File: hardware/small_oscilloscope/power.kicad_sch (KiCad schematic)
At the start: 16 parts, among them U10 EA2208T6R, U11 NE555P

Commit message: 250627 circuit
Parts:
- C3: renamed from C7; footprint (none) -> Capacitor_SMD:C_1206_3216Metric_Pad1.33x1.80mm_HandSolder
- C4: renamed from C8; footprint (none) -> Capacitor_SMD:C_0402_1005Metric_Pad0.74x0.62mm_HandSolder
- D1: renamed from D3; footprint Diode_SMD:D_MiniMELF_Handsoldering -> Diode_SMD:D_SOD-123
- D2: footprint Diode_SMD:D_MiniMELF_Handsoldering -> Diode_SMD:D_SOD-123
- D3: renamed from D1; footprint Diode_THT:D_DO-41_SOD81_P10.16mm_Horizontal -> Diode_SMD:D_SOD-123
- R24: footprint (none) -> Resistor_THT:R_Axial_DIN0207_L6.3mm_D2.5mm_P10.16mm_Horizontal
- R25: footprint (none) -> Capacitor_SMD:C_0402_1005Metric_Pad0.74x0.62mm_HandSolder
- renumbered C11 to C5, C10 to C6, C3 to C7, L2 to L1, R21 to R26, R22 to R27, U11 to U9
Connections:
- net +3.3V: no longer L1.1, U10.5 (NC)
- net 5V: now reaches U10.5 (NC)
- net 5V: now also L1.1

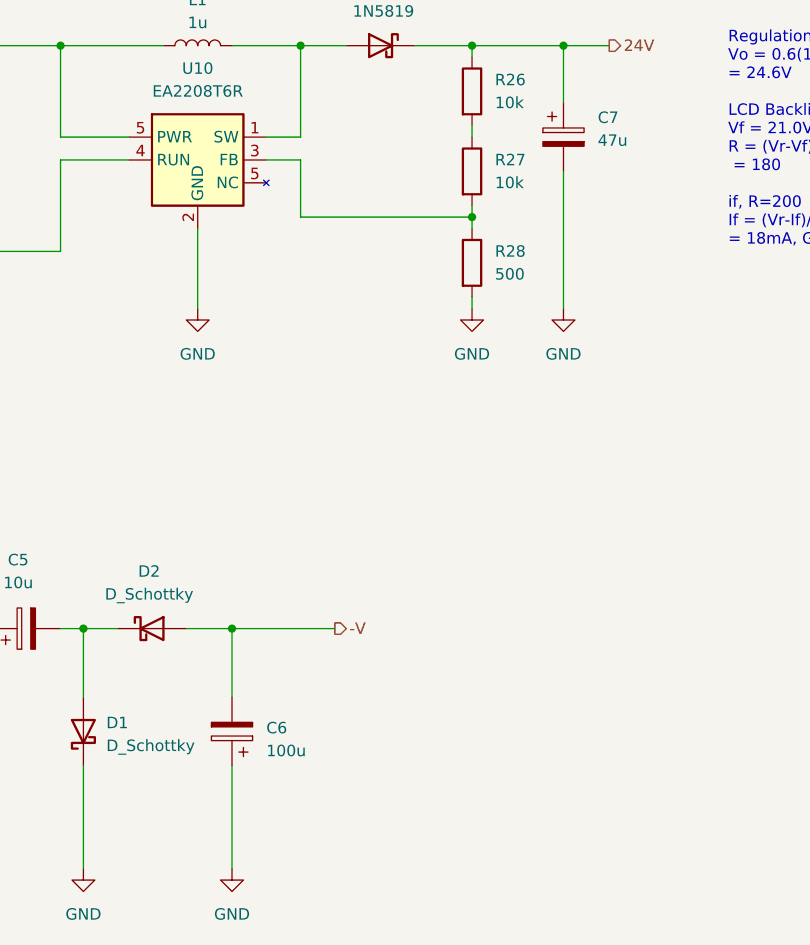
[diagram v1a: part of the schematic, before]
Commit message: feat: 오실로스코프 회로 설계 업데이트
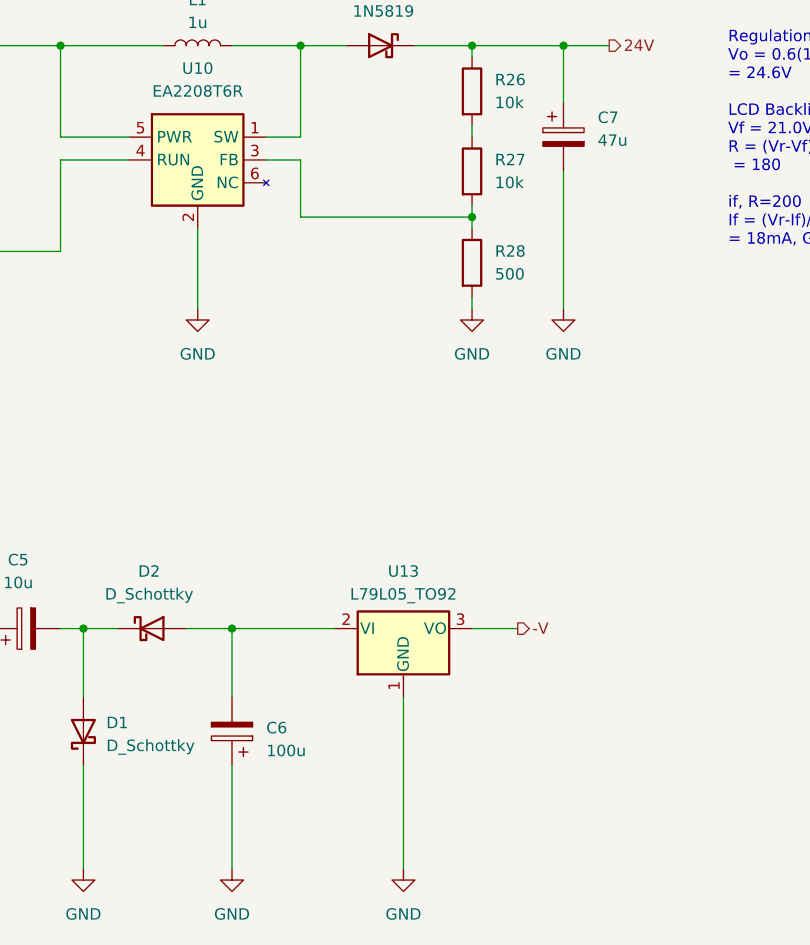
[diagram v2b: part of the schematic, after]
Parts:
- added U13: L79L05_TO92, Package_TO_SOT_THT:TO-92_Inline, symbol Regulator_Linear:L79L05_TO92
- C5: footprint Capacitor_THT:CP_Radial_D5.0mm_P2.00mm -> Capacitor_SMD:CP_Elec_4x5.7
- C6, C7: footprint Capacitor_THT:CP_Radial_D5.0mm_P2.00mm -> Capacitor_SMD:CP_Elec_6.3x5.7
- U9: footprint Package_SO:SOIC-8_3.9x4.9mm_P1.27mm -> Package_DIP:DIP-8_W7.62mm_LongPads
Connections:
- net -V: now also U13.3 (VO); no longer C6.2, D2.2 (A)
- net GND: now also U13.1 (GND)
- new net: C6.2, D2.2 (A), U13.2 (VI)
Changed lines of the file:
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@@
+	(wire
+		(pts
+			(xy 143.51 140.97) (xy 143.51 160.02)
+		)
+		(stroke
+			(width 0)
+			(type default)
+		)
+	)
 	(wire
 		(pts
@@
 		(pts
 			(xy 113.03 78.74) (xy 105.41 78.74)
+		)
+		(stroke
+			(width 0)
+			(type default)
+		)
+	)
+	(wire
+		(pts
+			(xy 151.13 133.35) (xy 156.21 133.35)
 		)
 		(stroke
@@
 	(hierarchical_label "-V"
 		(shape output)
-		(at 135.89 133.35 0)
+		(at 156.21 133.35 0)
 		(effects
 			(font
@@
 			)
 		)
-		(property "Footprint" "Capacitor_THT:CP_Radial_D5.0mm_P2.00mm"
+		(property "Footprint" "Capacitor_SMD:CP_Elec_6.3x5.7"
 			(at 123.4948 140.97 0)
 			(effects
@@
 			)
 		)
-		(property "Footprint" "Capacitor_THT:CP_Radial_D5.0mm_P2.00mm"
+		(property "Footprint" "Capacitor_SMD:CP_Elec_4x5.7"
 			(at 105.41 132.3848 0)
 			(effects
@@
 			)
 		)
-		(property "Footprint" "Package_SO:SOIC-8_3.9x4.9mm_P1.27mm"
+		(property "Footprint" "Package_DIP:DIP-8_W7.62mm_LongPads"
 			(at 97.79 143.51 0)
 			(effects
@@
 		(pin "2"
 		)
-		(pin "5"
+		(pin "6"
 		)
 		(instances
@@
 				(path "/722ad30e-a672-4959-92bf-662e54054c44/f6bdf31a-231a-4c5d-821c-5fbc6f0109a6"
 					(reference "#PWR047")
+					(unit 1)
+				)
+			)
+		)
+	)
+	(symbol
+		(lib_id "power:GND")
+		(at 143.51 160.02 0)
+		(unit 1)
+		(exclude_from_sim no)
+		(in_bom yes)
+		(on_board yes)
+		(dnp no)
+		(fields_autoplaced yes)
+		(property "Reference" "#PWR096"
+			(at 143.51 166.37 0)
+			(effects
+				(font
+					(size 1.27 1.27)
+				)
+				(hide yes)
+			)
+		)
+		(property "Value" "GND"
+			(at 143.51 165.1 0)
+			(effects
+				(font
+					(size 1.27 1.27)
+				)
+			)
+		)
+		(property "Footprint" ""
+			(at 143.51 160.02 0)
+			(effects
+				(font
+					(size 1.27 1.27)
+				)
+				(hide yes)
+			)
+		)
+		(property "Datasheet" ""
+			(at 143.51 160.02 0)
+			(effects
+				(font
+					(size 1.27 1.27)
+				)
+				(hide yes)
+			)
+		)
+		(property "Description" "Power symbol creates a global label with name \"GND\" , ground"
+			(at 143.51 160.02 0)
+			(effects
+				(font
+					(size 1.27 1.27)
+				)
+				(hide yes)
+			)
+		)
+		(pin "1"
+		)
+		(instances
+			(project "small_oscilloscope"
+				(path "/722ad30e-a672-4959-92bf-662e54054c44/f6bdf31a-231a-4c5d-821c-5fbc6f0109a6"
+					(reference "#PWR096")
 					(unit 1)
 				)
@@
 	)
 	(symbol
+		(lib_id "Regulator_Linear:L79L05_TO92")
+		(at 143.51 133.35 0)
+		(mirror x)
+		(unit 1)
+		(exclude_from_sim no)
+		(in_bom yes)
+		(on_board yes)
+		(dnp no)
+		(fields_autoplaced yes)
+		(property "Reference" "U13"
+			(at 143.51 127 0)
+			(effects
+				(font
+					(size 1.27 1.27)
+				)
+			)
+		)
+		(property "Value" "L79L05_TO92"
+			(at 143.51 129.54 0)
+			(effects
+				(font
+					(size 1.27 1.27)
+				)
+			)
+		)
+		(property "Footprint" "Package_TO_SOT_THT:TO-92_Inline"
+			(at 143.51 128.27 0)
+			(effects
+				(font
+					(size 1.27 1.27)
+					(italic yes)
+				)
+				(hide yes)
+			)
+		)
+		(property "Datasheet" "http://www.farnell.com/datasheets/1827870.pdf"
+			(at 143.51 133.35 0)
+			(effects
+				(font
+					(size 1.27 1.27)
+				)
+				(hide yes)
+			)
+		)
+		(property "Description" "Negative 100mA -30V Linear Regulator, Fixed Output -5V, TO-92"
+			(at 143.51 133.35 0)
+			(effects
+				(font
+					(size 1.27 1.27)
+				)
+				(hide yes)
+			)
+		)
+		(pin "2"
+		)
+		(pin "1"
+		)
+		(pin "3"
+		)
+		(instances
+			(project ""
+				(path "/722ad30e-a672-4959-92bf-662e54054c44/f6bdf31a-231a-4c5d-821c-5fbc6f0109a6"
+					(reference "U13")
+					(unit 1)
+				)
+			)
+		)
+	)
+	(symbol
 		(lib_id "power:GND")
 		(at 73.66 160.02 0)
@@
 			)
 		)
-		(property "Footprint" "Capacitor_THT:CP_Radial_D5.0mm_P2.00mm"
+		(property "Footprint" "Capacitor_SMD:CP_Elec_6.3x5.7"
 			(at 162.2552 82.55 0)
 			(effects

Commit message: oscilliscope first success
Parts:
- removed C3: 10n, Capacitor_SMD:C_1206_3216Metric_Pad1.33x1.80mm_HandSolder, symbol Device:C
- removed C4: 100n, Capacitor_SMD:C_0402_1005Metric_Pad0.74x0.62mm_HandSolder, symbol Device:C
- removed C6: 100u, Capacitor_SMD:CP_Elec_6.3x5.7, symbol Device:C_Polarized
- removed D1, D2: D_Schottky, Diode_SMD:D_SOD-123, symbol Device:D_Schottky
- removed R24: 560, Resistor_THT:R_Axial_DIN0207_L6.3mm_D2.5mm_P10.16mm_Horizontal, symbol Device:R
- removed R25: 4.7k, Capacitor_SMD:C_0402_1005Metric_Pad0.74x0.62mm_HandSolder, symbol Device:R
- removed R27: 10k, Resistor_THT:R_Axial_DIN0207_L6.3mm_D2.5mm_P10.16mm_Horizontal, symbol Device:R
- removed U13: L79L05_TO92, Package_TO_SOT_THT:TO-92_Inline, symbol Regulator_Linear:L79L05_TO92
- removed U9: NE555P, Package_DIP:DIP-8_W7.62mm_LongPads, symbol Timer:NE555P
- added C10: 10u, Capacitor_SMD:CP_Elec_6.3x5.7, symbol Device:C_Polarized
- added C7: 47u, Capacitor_SMD:CP_Elec_5x5.3, symbol Device:C_Polarized
- added C8: 100u, Capacitor_SMD:CP_Elec_5x5.3, symbol Device:C_Polarized
- added C9: 47u, Capacitor_SMD:CP_Elec_6.3x5.7, symbol Device:C_Polarized
- added D3, D6, D7: 1N5819, Diode_SMD:D_SOD-123, symbol Diode:1N5819
- added D4, D5: LED_Small, LED_THT:LED_D3.0mm, symbol Device:LED_Small
- added J4: BAT, Connector_PinSocket_2.54mm:PinSocket_1x02_P2.54mm_Vertical, symbol Connector:Conn_01x02_Socket
- added L2, L3, L4: 10u, Inductor_SMD:L_7.3x7.3_H3.5, symbol Device:L
- added L5: 100u, Inductor_SMD:L_7.3x7.3_H3.5, symbol Device:L
- added Q13: 2SC4671, Package_TO_SOT_SMD:SOT-523, symbol Transistor_BJT:2SC4213
- added R54, R56: 10k, Resistor_SMD:R_0402_1005Metric_Pad0.72x0.64mm_HandSolder, symbol Device:R
- added R57: 147k, Resistor_SMD:R_0402_1005Metric_Pad0.72x0.64mm_HandSolder, symbol Device:R
- added R58, R59, R61: 1k, Resistor_SMD:R_0603_1608Metric_Pad0.98x0.95mm_HandSolder, symbol Device:R
- added R60: 7.5k, Resistor_SMD:R_1206_3216Metric_Pad1.30x1.75mm_HandSolder, symbol Device:R
- added R62: 22k, Resistor_SMD:R_1206_3216Metric_Pad1.30x1.75mm_HandSolder, symbol Device:R
- added R63: 2.35k, Resistor_SMD:R_0402_1005Metric_Pad0.72x0.64mm_HandSolder, symbol Device:R
- added R64: 3k, Resistor_SMD:R_0402_1005Metric_Pad0.72x0.64mm_HandSolder, symbol Device:R
- added R65: 76.9R, Resistor_SMD:R_0402_1005Metric_Pad0.72x0.64mm_HandSolder, symbol Device:R
- added U10: EA8105, Package_TO_SOT_SMD:SOT-23-6, symbol Regulator_Switching:TPS62A01PDDC_1
- added U11: LM2576S-12, Package_TO_SOT_SMD:TO-263-5_TabPin3, symbol Regulator_Switching:LM2576S-12
- added U7, U9: EA2208T6R, Package_TO_SOT_SMD:SOT-23-6, symbol Regulator_Switching:TPS62A01PDDC
- added U8: TP4056-42-ESOP8, Package_SO:SOIC-8-1EP_3.9x4.9mm_P1.27mm_EP2.41x3.3mm_ThermalVias, symbol Battery_Management:TP4056-42-ESOP8
- C5: value 10u -> 100u; footprint Capacitor_SMD:CP_Elec_4x5.7 -> Capacitor_SMD:CP_Elec_5x5.3; now left out of the parts list
- C6: renamed from C7; value 47u -> 10u; footprint Capacitor_SMD:CP_Elec_6.3x5.7 -> Capacitor_SMD:CP_Elec_5x5.3; now left out of the parts list
- D2: renamed from D3; now left out of the parts list
- L1: value 1u -> 10u; footprint Inductor_SMD:L_Changjiang_FNR5045S -> Inductor_SMD:L_7.3x7.3_H3.5; now left out of the parts list
- R53: renamed from R26; value 10k -> 4.7k; footprint Resistor_THT:R_Axial_DIN0207_L6.3mm_D2.5mm_P10.16mm_Horizontal -> Resistor_SMD:R_0402_1005Metric_Pad0.72x0.64mm_HandSolder; now left out of the parts list
- R55: renamed from R28; value 500 -> 120; footprint Resistor_THT:R_Axial_DIN0207_L6.3mm_D2.5mm_P10.16mm_Horizontal -> Resistor_SMD:R_0402_1005Metric_Pad0.72x0.64mm_HandSolder; now left out of the parts list
- U6: renamed from U10; now left out of the parts list
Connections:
- net 5V is gone; now on net Vbat: L1.1, U6.5 (PWR)
- net +3.3V: now also C9.1, L4.2, R63.1
- net BACKLIGHT: now also R56.1; no longer U6.4 (RUN)
- net GND: now also C5.2, C10.1, C7.2, C8.2, C9.2, J4.2 (Pin_2), L5.2, Q13.2 (E), R60.2, R61.2, R64.2, R65.2, U10.2 (GND), U11.4 (FB), U7.2 (GND), U8.1 (TEMP), U8.3 (GND), U8.9 (EPAD), U9.2 (GND)
- net at R53.2: now also R55.1, U6.3 (FB)
- net Vbat: now reaches C5.1
- net Vbat: now also J4.1 (Pin_1), L2.1, L3.1, R54.1, U7.4 (RUN), U7.5 (PWR), U8.5 (BAT), U9.4 (RUN), U9.5 (PWR)
- new net: D6.2 (A), L3.2, U9.1 (SW)
- new net: L4.1, U10.3 (SW)
- new net: Q13.3 (C), R54.2, U6.4 (RUN)
- new net: D7.1 (K), L5.1, U11.2 (OUT)
- new net: D3.2 (A), L2.2, U7.1 (SW)
- new net: R63.2, R65.1, U10.6 (FBK)
- new net: R57.2, R60.1, U7.3 (FB)
- new net: D5.1 (K), R59.2
- new net: R62.2, R64.1, U9.3 (FB)
- new net: R61.1, U8.2 (PROG)
- new net: D4.1 (K), R58.2
- new net: Q13.1 (B), R56.2
- new net +12V: U11.1 (VIN)
- new net +5V: C8.1, D6.1 (K), R62.1, U10.1 (RUN), U10.4 (PWR)
- new net -12V: C10.2, D7.2 (A), U11.3 (GND), U11.5 (~{ON}/OFF)
- new net 12V: C7.1, D3.1 (K), R57.1
- new net Vusb: D4.2 (A), D5.2 (A), U8.4 (V_{CC}), U8.8 (CE)
- new net ~{CHRG}: R58.1, U8.7 (~{CHRG})
- new net ~{STDBY}: R59.1, U8.6 (~{STDBY})
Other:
- note added: "# 최종 확정 사항 ## 전원 - 상시 전원 공급 Source : VBAT=2.7 ~ 4.2 - BAT 충전 : 5V -> VBAT=4.2 (TP4056) - 배터리 승압 회로 : VBAT -> 5V (EA2208) - 양전압 생성 회로 : VBAT -> 12V (EA2208) - 음전압 생성 회로 : 12V -> -12V (LM2576) - 백라이트 회로 : VBAT -> 24V (EA2208) - 강하 회로 : 5V -> 3.3V (EA8105)"
- note added: "-12V Generator Inverting Buck-Boost Regulator of LM2576's datasheet"
- note added: "12V Generator Regulation Notes Vo = 0.6(1+R1/R2), R1/R2 = 19 = 12.0V R1 = 147k R2 = 7.5k"
- note added: "1K = 1.2A"
- note added: "24V Generator Regulation Notes Vo = 0.6(1+R1/R2), R1/R2 = 39.17 = 24.1V LCD Backlight Notes Vf = 21.0V, If = 20mA, Vreg = 24.1V R = (Vr-Vf)/If = 155 if, R=150 If = (Vr-If)/R = 20.7mA, Good."
- note added: "3V3 Generator Regulation Notes Vo = 0.6(1+R1/R2), R1/R2 = 4.5 = 3.3V R1 = 470k R2 = 100k"
- note added: "5V Generator Regulation Notes Vo = 0.6(1+R1/R2), R1/R2 = 7.333 = 5.0V R1 = 22k R2 = 3k"
- note removed: "Input : 3.7V bat input Features: 1. Battery Charging Unit (already in module) 2. +5V Generator (already in module) 3. -5V Generator 4. LED Backlight(+21V) Generator 5. Battery gauge(self-measurement)"
- note removed: "Regulation Notes Vo = 0.6(1+R1/R2), R1/R2 = 40 = 24.6V LCD Backlight Notes Vf = 21.0V, If = 20mA, Vreg = 24.6V R = (Vr-Vf)/If = 180 if, R=200 If = (Vr-If)/R = 18mA, Good."
- moved on the sheet: C6, D2, L1, R53, R55, U6

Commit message: fix: program tidy
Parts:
- added Q19, Q20, Q21: Q_NPN_EBC, Package_TO_SOT_SMD:SOT-323_SC-70, symbol Transistor_BJT:Q_NPN_EBC
- added Q22: 2N3906, Package_TO_SOT_THT:TO-92_Inline, symbol Transistor_BJT:2N3906
- added R100, R102, R104, R99: 100k, symbol Device:R
- added R101, R103: 10k, symbol Device:R
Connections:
- net +5V: now also Q22.1 (E), R100.1, R99.1
- net -12V: now also Q19.1 (E), Q20.1 (E); no longer U11.5 (~{ON}/OFF)
- net GND: now also Q21.1 (E)
- new net: Q19.2 (B), R103.2
- new net: Q19.3 (C), Q22.3 (C), R101.1, U11.5 (~{ON}/OFF)
- new net: Q21.2 (B), R102.2
- new net: Q20.2 (B), R101.2
- new net: Q20.3 (C), R100.2, R103.1
- new net: Q22.2 (B), R104.2, R99.2
- new net: Q21.3 (C), R104.1
- new net Qvsec: R102.1
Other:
- moved on the sheet: C10, D7, L5, U11
